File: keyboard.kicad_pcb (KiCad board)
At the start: 2 copper layers, 285 x 94.6 mm, 208 parts, among them J1 USB_C_Receptacle_USB2.0, J2 -, J3 -, K1 SW, K2 SW, P1 SWD, P2 BATT, U1 nRF52810-ND04C, U2 CH554T, U3 TP4057, U4 XC6206P30

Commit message: 增加顶部电池P2.0接口，修改LED为RGBA封装，避免优信店内LED需要反装的问题。微调LOGO位置
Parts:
- added G***: LOGO, Customv2:Cirno_38113046_mask, B.Cu at (230.3, 150.0)
- added P3: BATT, Connector_PinSocket_2.00mm:PinSocket_1x02_P2.00mm_Vertical, B.Cu at (214.3, 81.9)
- moved G*** 0.13 mm to (225.5, 148.1)
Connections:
- D104 pad 2: 3V3 -> Net-(D102-Pad2)
- D104 pad 4: Net-(D102-Pad2) -> 3V3
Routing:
- net BATT: track 99.5 -> 171.9 mm
- net Net-(D102-Pad2): track 46.1 -> 52.0 mm
- net 3V3: track 237.4 -> 240.2 mm, vias 4 -> 5
- net GND: track 299.7 -> 301.7 mm
- net Net-(D103-Pad2): track 69.9 -> 70.8 mm
- net UART_RX: track 31.0 -> 31.5 mm
- net UART_TX: track 30.3 -> 30.8 mm
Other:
- board text added: "Lot60-BLE Rev.E https://wiki.lotlab.org"
- board text added: "PixivID: 38113046"
- board text removed: "Lot60-BLE Rev.E Document: wiki.lotlab.org"

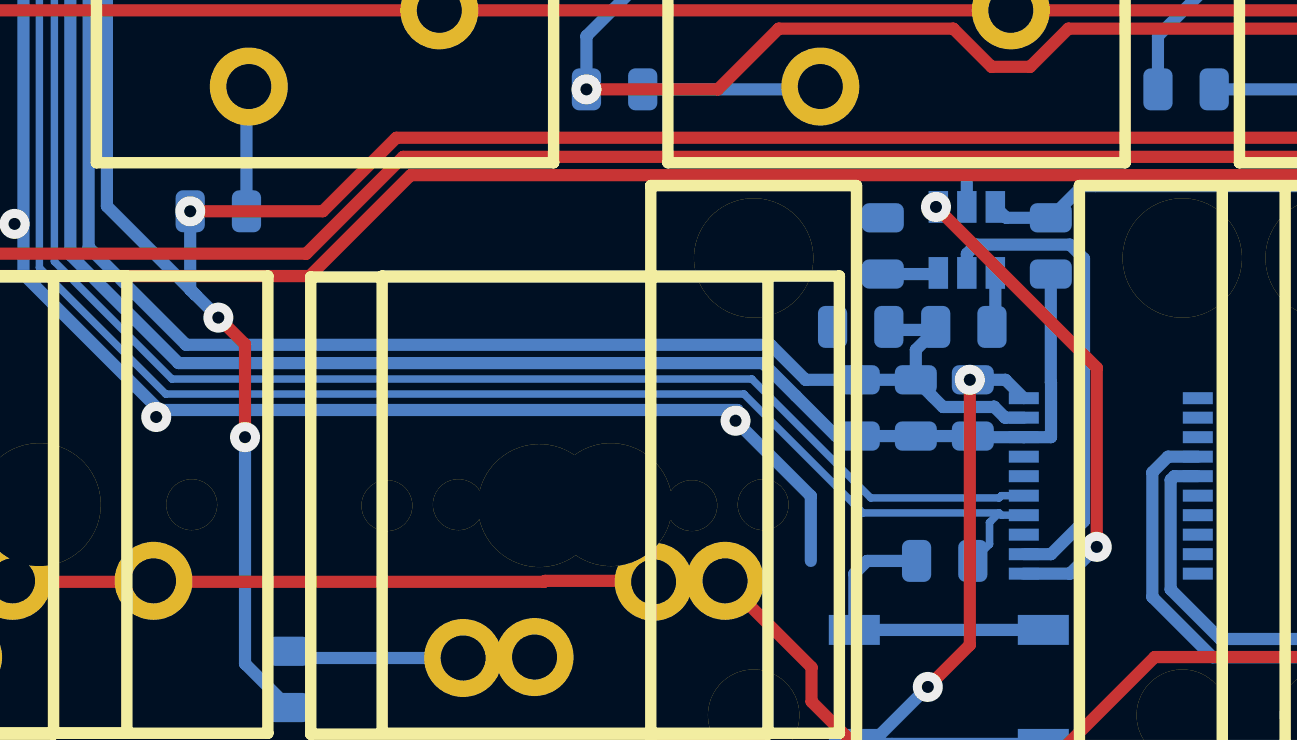
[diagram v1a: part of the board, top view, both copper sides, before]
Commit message: 将SS14封装更换为更易买到的SMA，将XC6206P30换为更易买到的XC6206P33
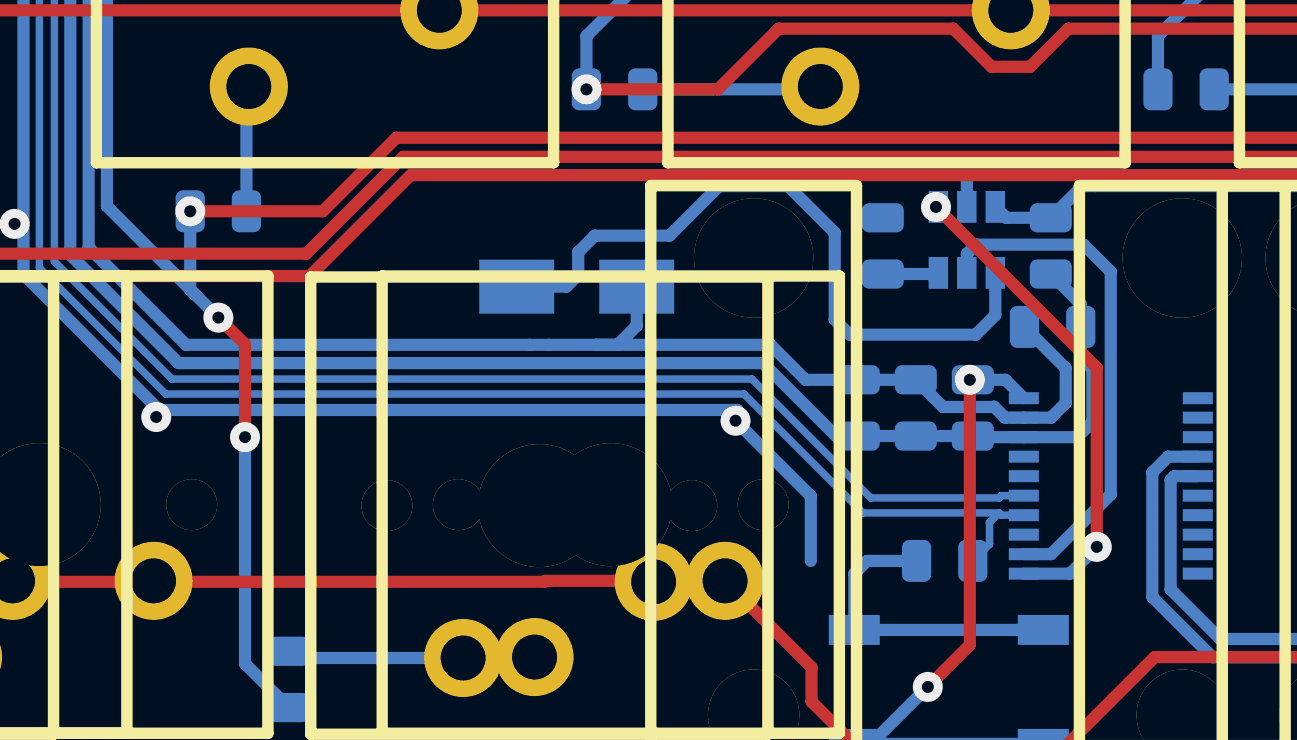
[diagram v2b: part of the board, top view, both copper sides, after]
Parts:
- D104: value LED_CRGB -> FM-3528RGBA
- D20: footprint Diode_SMD:D_0805_2012Metric -> Diode_SMD:D_SMA
- U4: value XC6206P30 -> XC6206P33
- moved D20 13.0 mm to (122.7, 142.7), turned to 0 degrees
- moved C2 6.40 mm to (138.6, 144.1), turned to 0 degrees
- moved G*** 0.75 mm to (229.6, 149.8)
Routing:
- net Net-(D20-Pad1): track 1.85 -> 23.2 mm
- net VCC: track 137.9 -> 142.1 mm
- net GND: track 301.7 -> 303.4 mm
- net STBY: track 16.1 -> 17.1 mm

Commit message: 为蓝牙模块天线位置添加开孔，修改GPIO接口位置
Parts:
- J3: moved to B.Cu
- moved J3 40.8 mm to (191.4, 140.5), turned to 270 degrees
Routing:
- net /GPIO1: track 3.20 -> 44.7 mm, vias 0 -> 1
- net GND: track 303.4 -> 320.0 mm, vias 14 -> 15
- net /GPIO2: track 114.4 -> 126.2 mm, vias 4 -> 3
- net 3V3: track 240.2 -> 251.6 mm, vias 5 -> 6
- net /GPIO0: track 21.1 -> 30.4 mm
- net UART_RX: track 31.5 -> 25.9 mm
- net UART_TX: track 30.8 -> 27.4 mm
- net /row5: track 439.7 -> 437.7 mm
- net BATT: track 171.9 -> 173.9 mm
- net /row4: track 332.0 -> 333.9 mm
- net /row3: track 344.2 -> 345.5 mm
- net /col5: track 119.3 -> 118.0 mm
- net /col1: track 192.6 -> 193.8 mm
- net /col2: track 176.7 -> 177.8 mm
- net /col3: track 167.5 -> 168.7 mm
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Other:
- outline, holes or cut-outs redrawn
- board text added: "GPIO"

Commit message: 修正阵列二极管在原理图上的方向与封装方向不一致的问题
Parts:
- moved D15 1.21 mm to (114.1, 155.1), turned to 180 degrees
- turned D1 to 180 degrees
- turned D10 to 180 degrees
- turned D11 to 180 degrees
- turned D12 to 180 degrees
- turned D13 to 180 degrees
- turned D14 to 180 degrees
- turned D16 to 180 degrees
- turned D17 to 180 degrees
- turned D18 to 180 degrees
- turned D19 to 180 degrees
- turned D2 to 180 degrees
- turned D21 to 180 degrees
- turned D22 to 180 degrees
- turned D23 to 180 degrees
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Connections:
- D1 pad 1: /col1 -> Net-(D1-Pad1)
- D1 pad 2: Net-(D1-Pad2) -> /col1
- D10 pad 1: /col2 -> Net-(D10-Pad1)
- D10 pad 2: Net-(D10-Pad2) -> /col2
- D100 pad 1: Net-(D100-Pad1) -> GND
- D100 pad 2: GND -> Net-(D100-Pad2)
- D1001 pad 1: Net-(D100-Pad1) -> GND
- D1001 pad 2: GND -> Net-(D100-Pad2)
- D1002 pad 1: Net-(D100-Pad1) -> GND
- D1002 pad 2: GND -> Net-(D100-Pad2)
- D11 pad 1: /col3 -> Net-(D11-Pad1)
- D11 pad 2: Net-(D11-Pad2) -> /col3
- D12 pad 1: /col3 -> Net-(D12-Pad1)
- D12 pad 2: Net-(D12-Pad2) -> /col3
- D13 pad 1: /col3 -> Net-(D13-Pad1)
- D13 pad 2: Net-(D13-Pad2) -> /col3
- D14 pad 1: /col3 -> Net-(D14-Pad1)
- D14 pad 2: Net-(D14-Pad2) -> /col3
- D15 pad 1: /col3 -> Net-(D15-Pad1)
- D15 pad 2: Net-(D15-Pad2) -> /col3
- D16 pad 1: /col4 -> Net-(D16-Pad1)
- D16 pad 2: Net-(D16-Pad2) -> /col4
- D17 pad 1: /col4 -> Net-(D17-Pad1)
- D17 pad 2: Net-(D17-Pad2) -> /col4
- D18 pad 1: /col4 -> Net-(D18-Pad1)
- D18 pad 2: Net-(D18-Pad2) -> /col4
- D19 pad 1: /col4 -> Net-(D19-Pad1)
- D19 pad 2: Net-(D19-Pad2) -> /col4
- D2 pad 1: /col1 -> Net-(D2-Pad1)
- D2 pad 2: Net-(D2-Pad2) -> /col1
- D21 pad 1: /col5 -> Net-(D21-Pad1)
- D21 pad 2: Net-(D21-Pad2) -> /col5
- D22 pad 1: /col5 -> Net-(D22-Pad1)
- D22 pad 2: Net-(D22-Pad2) -> /col5
- D23 pad 1: /col5 -> Net-(D23-Pad1)
- D23 pad 2: Net-(D23-Pad2) -> /col5
- D24 pad 1: /col5 -> Net-(D24-Pad1)
- D24 pad 2: Net-(D24-Pad2) -> /col5
- D26 pad 1: /col6 -> Net-(D26-Pad1)
- D26 pad 2: Net-(D26-Pad2) -> /col6
- D27 pad 1: /col6 -> Net-(D27-Pad1)
- D27 pad 2: Net-(D27-Pad2) -> /col6
- D28 pad 1: /col6 -> Net-(D28-Pad1)
- D28 pad 2: Net-(D28-Pad2) -> /col6
- D29 pad 1: /col6 -> Net-(D29-Pad1)
- D29 pad 2: Net-(D29-Pad2) -> /col6
- D3 pad 1: /col1 -> Net-(D3-Pad1)
- D3 pad 2: Net-(D3-Pad2) -> /col1
- D30 pad 1: /col6 -> Net-(D30-Pad1)
- D30 pad 2: Net-(D30-Pad2) -> /col6
- D31 pad 1: /col7 -> Net-(D31-Pad1)
- D31 pad 2: Net-(D31-Pad2) -> /col7
- D32 pad 1: /col7 -> Net-(D32-Pad1)
- D32 pad 2: Net-(D32-Pad2) -> /col7
- D33 pad 1: /col7 -> Net-(D33-Pad1)
- D33 pad 2: Net-(D33-Pad2) -> /col7
- D34 pad 1: /col7 -> Net-(D34-Pad1)
- D34 pad 2: Net-(D34-Pad2) -> /col7
- D36 pad 1: /col8 -> Net-(D36-Pad1)
- D36 pad 2: Net-(D36-Pad2) -> /col8
- D37 pad 1: /col8 -> Net-(D37-Pad1)
- D37 pad 2: Net-(D37-Pad2) -> /col8
- D38 pad 1: /col8 -> Net-(D38-Pad1)
- D38 pad 2: Net-(D38-Pad2) -> /col8
- D39 pad 1: /col8 -> Net-(D39-Pad1)
- D39 pad 2: Net-(D39-Pad2) -> /col8
- D4 pad 1: /col1 -> Net-(D4-Pad1)
- D4 pad 2: Net-(D4-Pad2) -> /col1
- D41 pad 1: /col9 -> Net-(D41-Pad1)
- D41 pad 2: Net-(D41-Pad2) -> /col9
- D42 pad 1: /col9 -> Net-(D42-Pad1)
- D42 pad 2: Net-(D42-Pad2) -> /col9
- D43 pad 1: /col9 -> Net-(D43-Pad1)
- D43 pad 2: Net-(D43-Pad2) -> /col9
- D44 pad 1: /col9 -> Net-(D44-Pad1)
- D44 pad 2: Net-(D44-Pad2) -> /col9
- D46 pad 1: /col10 -> Net-(D46-Pad1)
- D46 pad 2: Net-(D46-Pad2) -> /col10
- D47 pad 1: /col10 -> Net-(D47-Pad1)
- D47 pad 2: Net-(D47-Pad2) -> /col10
- D48 pad 1: /col10 -> Net-(D48-Pad1)
- D48 pad 2: Net-(D48-Pad2) -> /col10
- D49 pad 1: /col10 -> Net-(D49-Pad1)
- D49 pad 2: Net-(D49-Pad2) -> /col10
- D5 pad 1: /col1 -> Net-(D5-Pad1)
- D5 pad 2: Net-(D5-Pad2) -> /col1
- D50 pad 1: /col10 -> Net-(D50-Pad1)
- D50 pad 2: Net-(D50-Pad2) -> /col10
- D51 pad 1: /col11 -> Net-(D51-Pad1)
- D51 pad 2: Net-(D51-Pad2) -> /col11
- D52 pad 1: /col11 -> Net-(D52-Pad1)
- D52 pad 2: Net-(D52-Pad2) -> /col11
- D53 pad 1: /col11 -> Net-(D53-Pad1)
- D53 pad 2: Net-(D53-Pad2) -> /col11
- D54 pad 1: /col11 -> Net-(D54-Pad1)
- D54 pad 2: Net-(D54-Pad2) -> /col11
- D55 pad 1: /col11 -> Net-(D55-Pad1)
- D55 pad 2: Net-(D55-Pad2) -> /col11
- D56 pad 1: /col12 -> Net-(D56-Pad1)
- D56 pad 2: Net-(D56-Pad2) -> /col12
- D57 pad 1: /col12 -> Net-(D57-Pad1)
- D57 pad 2: Net-(D57-Pad2) -> /col12
- D58 pad 1: /col12 -> Net-(D58-Pad1)
- D58 pad 2: Net-(D58-Pad2) -> /col12
- D59 pad 1: /col12 -> Net-(D59-Pad1)
- D59 pad 2: Net-(D59-Pad2) -> /col12
- D6 pad 1: /col2 -> Net-(D6-Pad1)
- D6 pad 2: Net-(D6-Pad2) -> /col2
- D60 pad 1: /col12 -> Net-(D60-Pad1)
- D60 pad 2: Net-(D60-Pad2) -> /col12
- D61 pad 1: /col13 -> Net-(D61-Pad1)
- D61 pad 2: Net-(D61-Pad2) -> /col13
- D62 pad 1: /col13 -> Net-(D62-Pad1)
- D62 pad 2: Net-(D62-Pad2) -> /col13
- D63 pad 1: /col13 -> Net-(D63-Pad1)
- D63 pad 2: Net-(D63-Pad2) -> /col13
- D64 pad 1: /col13 -> Net-(D64-Pad1)
- D64 pad 2: Net-(D64-Pad2) -> /col13
- D65 pad 1: /col13 -> Net-(D65-Pad1)
- D65 pad 2: Net-(D65-Pad2) -> /col13
- D66 pad 1: /col14 -> Net-(D66-Pad1)
- D66 pad 2: Net-(D66-Pad2) -> /col14
- D67 pad 1: /col14 -> Net-(D67-Pad1)
- D67 pad 2: Net-(D67-Pad2) -> /col14
- D68 pad 1: /col14 -> Net-(D68-Pad1)
- D68 pad 2: Net-(D68-Pad2) -> /col14
- D69 pad 1: /col14 -> Net-(D69-Pad1)
- D69 pad 2: Net-(D69-Pad2) -> /col14
- D7 pad 1: /col2 -> Net-(D7-Pad1)
- D7 pad 2: Net-(D7-Pad2) -> /col2
- D70 pad 1: /col14 -> Net-(D70-Pad1)
- D70 pad 2: Net-(D70-Pad2) -> /col14
- D8 pad 1: /col2 -> Net-(D8-Pad1)
- D8 pad 2: Net-(D8-Pad2) -> /col2
- D9 pad 1: /col2 -> Net-(D9-Pad1)
- D9 pad 2: Net-(D9-Pad2) -> /col2
- R100 pad 2: Net-(D100-Pad1) -> Net-(D100-Pad2)
- S1 pad 2: Net-(D1-Pad2) -> Net-(D1-Pad1)
- S10 pad 2: Net-(D10-Pad2) -> Net-(D10-Pad1)
- S101 pad 2: Net-(D10-Pad2) -> Net-(D10-Pad1)
- S102 pad 2: Net-(D10-Pad2) -> Net-(D10-Pad1)
- S11 pad 2: Net-(D11-Pad2) -> Net-(D11-Pad1)
- S12 pad 2: Net-(D12-Pad2) -> Net-(D12-Pad1)
- S13 pad 2: Net-(D13-Pad2) -> Net-(D13-Pad1)
- S14 pad 2: Net-(D14-Pad2) -> Net-(D14-Pad1)
- S15 pad 2: Net-(D15-Pad2) -> Net-(D15-Pad1)
- S151 pad 2: Net-(D15-Pad2) -> Net-(D15-Pad1)
- S16 pad 2: Net-(D16-Pad2) -> Net-(D16-Pad1)
- S17 pad 2: Net-(D17-Pad2) -> Net-(D17-Pad1)
- S18 pad 2: Net-(D18-Pad2) -> Net-(D18-Pad1)
- S19 pad 2: Net-(D19-Pad2) -> Net-(D19-Pad1)
- S2 pad 2: Net-(D2-Pad2) -> Net-(D2-Pad1)
- S21 pad 2: Net-(D21-Pad2) -> Net-(D21-Pad1)
- S22 pad 2: Net-(D22-Pad2) -> Net-(D22-Pad1)
- S23 pad 2: Net-(D23-Pad2) -> Net-(D23-Pad1)
- S24 pad 2: Net-(D24-Pad2) -> Net-(D24-Pad1)
- S26 pad 2: Net-(D26-Pad2) -> Net-(D26-Pad1)
- S27 pad 2: Net-(D27-Pad2) -> Net-(D27-Pad1)
- S28 pad 2: Net-(D28-Pad2) -> Net-(D28-Pad1)
- S29 pad 2: Net-(D29-Pad2) -> Net-(D29-Pad1)
- S3 pad 2: Net-(D3-Pad2) -> Net-(D3-Pad1)
- S30 pad 2: Net-(D30-Pad2) -> Net-(D30-Pad1)
- S3001 pad 1: Net-(D3-Pad2) -> Net-(D3-Pad1)
- S301 pad 2: Net-(D30-Pad2) -> Net-(D30-Pad1)
- S302 pad 2: Net-(D30-Pad2) -> Net-(D30-Pad1)
- S31 pad 2: Net-(D31-Pad2) -> Net-(D31-Pad1)
- S32 pad 2: Net-(D32-Pad2) -> Net-(D32-Pad1)
- S33 pad 2: Net-(D33-Pad2) -> Net-(D33-Pad1)
- S34 pad 2: Net-(D34-Pad2) -> Net-(D34-Pad1)
- S36 pad 2: Net-(D36-Pad2) -> Net-(D36-Pad1)
- S37 pad 2: Net-(D37-Pad2) -> Net-(D37-Pad1)
- S38 pad 2: Net-(D38-Pad2) -> Net-(D38-Pad1)
- S39 pad 2: Net-(D39-Pad2) -> Net-(D39-Pad1)
- S4 pad 2: Net-(D4-Pad2) -> Net-(D4-Pad1)
- S4001 pad 2: Net-(D4-Pad2) -> Net-(D4-Pad1)
- S41 pad 2: Net-(D41-Pad2) -> Net-(D41-Pad1)
- S42 pad 2: Net-(D42-Pad2) -> Net-(D42-Pad1)
- S43 pad 2: Net-(D43-Pad2) -> Net-(D43-Pad1)
- S44 pad 2: Net-(D44-Pad2) -> Net-(D44-Pad1)
- S46 pad 2: Net-(D46-Pad2) -> Net-(D46-Pad1)
- S47 pad 2: Net-(D47-Pad2) -> Net-(D47-Pad1)
- S48 pad 2: Net-(D48-Pad2) -> Net-(D48-Pad1)
- S49 pad 2: Net-(D49-Pad2) -> Net-(D49-Pad1)
- S5 pad 2: Net-(D5-Pad2) -> Net-(D5-Pad1)
- S50 pad 2: Net-(D50-Pad2) -> Net-(D50-Pad1)
- S51 pad 2: Net-(D51-Pad2) -> Net-(D51-Pad1)
- S512 pad 2: Net-(D5-Pad2) -> Net-(D5-Pad1)
- S52 pad 2: Net-(D52-Pad2) -> Net-(D52-Pad1)
- S53 pad 2: Net-(D53-Pad2) -> Net-(D53-Pad1)
- S54 pad 2: Net-(D54-Pad2) -> Net-(D54-Pad1)
- S55 pad 2: Net-(D55-Pad2) -> Net-(D55-Pad1)
- S552 pad 2: Net-(D55-Pad2) -> Net-(D55-Pad1)
- S56 pad 2: Net-(D56-Pad2) -> Net-(D56-Pad1)
- S57 pad 2: Net-(D57-Pad2) -> Net-(D57-Pad1)
- S58 pad 2: Net-(D58-Pad2) -> Net-(D58-Pad1)
- S59 pad 2: Net-(D59-Pad2) -> Net-(D59-Pad1)
- S6 pad 2: Net-(D6-Pad2) -> Net-(D6-Pad1)
- S60 pad 2: Net-(D60-Pad2) -> Net-(D60-Pad1)
- S601 pad 2: Net-(D60-Pad2) -> Net-(D60-Pad1)
- S602 pad 2: Net-(D60-Pad2) -> Net-(D60-Pad1)
- S61 pad 2: Net-(D61-Pad2) -> Net-(D61-Pad1)
- S62 pad 2: Net-(D62-Pad2) -> Net-(D62-Pad1)
- S63 pad 2: Net-(D63-Pad2) -> Net-(D63-Pad1)
- S64 pad 1: Net-(D64-Pad2) -> Net-(D64-Pad1)
- S641 pad 2: Net-(D64-Pad2) -> Net-(D64-Pad1)
- S65 pad 2: Net-(D65-Pad2) -> Net-(D65-Pad1)
- S6512 pad 2: Net-(D65-Pad2) -> Net-(D65-Pad1)
- S66 pad 2: Net-(D66-Pad2) -> Net-(D66-Pad1)
- S661 pad 2: Net-(D66-Pad2) -> Net-(D66-Pad1)
- S67 pad 2: Net-(D67-Pad2) -> Net-(D67-Pad1)
- S68 pad 2: Net-(D68-Pad2) -> Net-(D68-Pad1)
- S681 pad 2: Net-(D68-Pad2) -> Net-(D68-Pad1)
- S682 pad 1: Net-(D68-Pad2) -> Net-(D68-Pad1)
- S69 pad 2: Net-(D69-Pad2) -> Net-(D69-Pad1)
- S691 pad 1: Net-(D69-Pad2) -> Net-(D69-Pad1)
- S692 pad 2: Net-(D69-Pad2) -> Net-(D69-Pad1)
- S7 pad 2: Net-(D7-Pad2) -> Net-(D7-Pad1)
- S70 pad 2: Net-(D70-Pad2) -> Net-(D70-Pad1)
- S7012 pad 2: Net-(D70-Pad2) -> Net-(D70-Pad1)
- S8 pad 2: Net-(D8-Pad2) -> Net-(D8-Pad1)
- S9 pad 2: Net-(D9-Pad2) -> Net-(D9-Pad1)
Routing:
- net Net-(D64-Pad2): track 38.1 -> 0.00 mm, vias 2 -> 0
- net Net-(D64-Pad1): track 0.00 -> 38.1 mm, vias 0 -> 2
- net Net-(D68-Pad2): track 32.3 -> 0.00 mm
- net Net-(D68-Pad1): track 0.00 -> 32.3 mm
- net Net-(D69-Pad2): track 30.1 -> 0.00 mm
- net Net-(D69-Pad1): track 0.00 -> 30.1 mm
- net Net-(D30-Pad2): track 26.4 -> 0.00 mm
- net Net-(D30-Pad1): track 0.00 -> 26.4 mm
- net Net-(D100-Pad2): track 0.00 -> 17.8 mm
- net Net-(D4-Pad2): track 17.6 -> 0.00 mm
- net Net-(D4-Pad1): track 0.00 -> 17.6 mm
- net Net-(D3-Pad2): track 17.5 -> 0.00 mm
- net Net-(D3-Pad1): track 0.00 -> 17.5 mm
- net Net-(D100-Pad1): track 14.7 -> 0.00 mm
- net Net-(D29-Pad2): track 13.7 -> 0.00 mm, vias 1 -> 0
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
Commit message: 移动二极管位置以增强外壳兼容性
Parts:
- moved D55 14.0 mm to (256.7, 141.2)
- moved D60 10.6 mm to (280.0, 145.2)
- moved D70 10.2 mm to (327.4, 145.5)
- moved D65 9.51 mm to (303.7, 146.3)
- moved D64 7.94 mm to (299.3, 133.7)
- moved D4 6.73 mm to (67.3, 134.6)
- moved D3 6.52 mm to (67.4, 115.2)
- moved D5 6.37 mm to (67.9, 146.6)
- moved D12 5.64 mm to (120.6, 99.2)
- moved D29 4.29 mm to (177.1, 137.3)
- moved D30 3.92 mm to (179.7, 155.2), turned to 180 degrees
- moved D54 3.71 mm to (260.7, 136.1)
- moved D49 3.60 mm to (241.7, 136.7)
- moved D14 3.60 mm to (108.3, 137.5)
- moved D24 3.51 mm to (146.5, 136.1)
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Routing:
- net Net-(D55-Pad1): track 7.79 -> 18.9 mm
- net /col3: track 167.4 -> 178.5 mm
- net /col12: track 198.2 -> 188.7 mm
- net /col11: track 173.9 -> 165.8 mm
- net Net-(D5-Pad1): track 7.68 -> 14.1 mm
- net Net-(D60-Pad1): track 10.7 -> 16.9 mm
- net /col13: track 213.7 -> 219.7 mm
- net Net-(D70-Pad1): track 8.37 -> 14.1 mm
- net Net-(D65-Pad1): track 8.44 -> 13.6 mm
- net GND: track 320.0 -> 325.1 mm, vias 15 -> 14
- net Net-(D12-Pad1): track 3.78 -> 8.65 mm
- net Net-(D30-Pad1): track 26.4 -> 21.6 mm
- net Net-(D4-Pad1): track 17.6 -> 13.1 mm
- net Net-(D54-Pad1): track 6.59 -> 2.58 mm
- net Net-(D49-Pad1): track 6.60 -> 2.74 mm
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
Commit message: 改进了空格和左GUI键的接线顺序，使其更难粘连
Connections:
- S102 pad 1: /row5 -> Net-(D10-Pad1)
- S102 pad 2: Net-(D10-Pad1) -> /row5
- S30 pad 1: /row5 -> Net-(D30-Pad1)
- S30 pad 2: Net-(D30-Pad1) -> /row5
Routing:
- net /row5: track 439.3 -> 448.6 mm
- net Net-(D10-Pad1): track 9.76 -> 18.7 mm
- net Net-(D30-Pad1): track 21.6 -> 30.4 mm
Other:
- board text added: "Lot60-BLE Rev.F https://wiki.lotlab.org"
- board text added: "©2018-2019"
- board text removed: "Lot60-BLE Rev.E https://wiki.lotlab.org"
- board text removed: "©2012-2019"

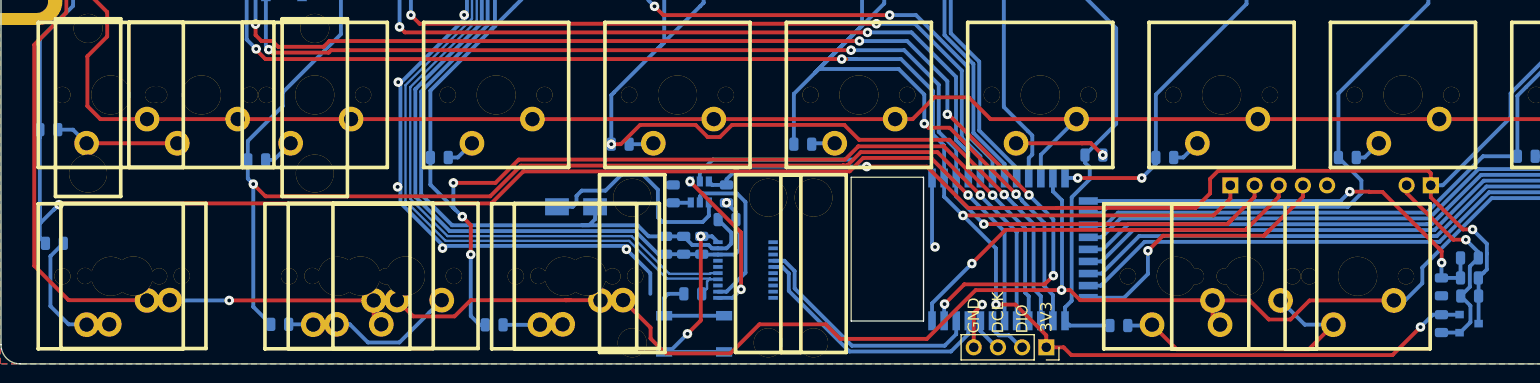
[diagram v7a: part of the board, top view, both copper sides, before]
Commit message: 改进供电部分，现在支持仅USB供电了
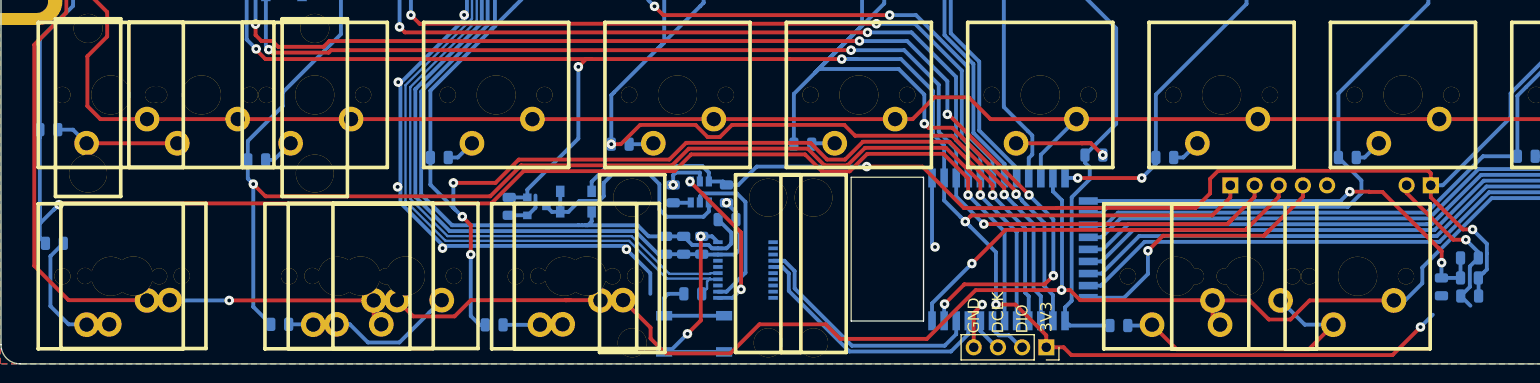
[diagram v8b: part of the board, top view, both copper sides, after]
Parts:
- added D25: B5819W SL, Diode_SMD:D_SOD-123, B.Cu at (122.7, 143.3)
- D20: value SS14 -> B5819W SL; footprint Diode_SMD:D_SMA -> Diode_SMD:D_SOD-123
- moved U4 98.7 mm to (118.6, 142.7)
- moved C6 98.7 mm to (115.7, 142.7)
- moved D20 1.62 mm to (122.7, 141.1)
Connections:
- D20 pad 2: VCC -> BATT
- U4 pad 3: BATT -> Net-(D20-Pad1)
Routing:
- net 3V3: track 252.1 -> 268.3 mm, vias 6 -> 7
- net GND: track 325.1 -> 311.6 mm, vias 14 -> 15
- net BATT: track 171.4 -> 183.3 mm
- net Net-(D20-Pad1): track 23.2 -> 26.7 mm
- net /col1: track 190.5 -> 193.3 mm
- net /col2: track 178.7 -> 181.3 mm
- net /col3: track 178.1 -> 180.6 mm
- net VCC: track 144.6 -> 143.5 mm
